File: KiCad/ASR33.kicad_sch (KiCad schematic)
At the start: 42 parts, among them J1 USB-C, J2 DC, J3 Power, J4 RUN, J5 Tx, J6 Rx, Q1 NX7002AK, SW1 SW_Push, U1 ESP32-WROOM-32, U2 FT231XQ, U3 NCR402U, U4 NCR402U, U5 LTV-355T, U6 LMR16006+FB, U7 QR

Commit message: Diode
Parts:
- D4: value D -> Schottky
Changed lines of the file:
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@@
     (in_bom yes) (on_board yes) (fields_autoplaced)
     (property "Reference" "D4" (id 0) (at 194.945 20.1635 0))
-    (property "Value" "D" (id 1) (at 194.945 22.9386 0))
+    (property "Value" "Schottky" (id 1) (at 194.945 22.9386 0))
     (property "Footprint" "Diode_SMD:D_1206_3216Metric" (id 2) (at 194.945 25.4 0)
       (effects (font (size 1.27 1.27)) hide)
@@
     )
     (path "/c30cd6e9-8158-45a7-96ab-d9fa2290e882"
-      (reference "D4") (unit 1) (value "D") (footprint "Diode_SMD:D_1206_3216Metric")
+      (reference "D4") (unit 1) (value "Schottky") (footprint "Diode_SMD:D_1206_3216Metric")
     )
     (path "/00000000-0000-0000-0000-0000610fe5d2"

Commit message: More tinkering
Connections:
- net MTR: now also U1.36 (IO22); no longer U1.37 (IO23)
- net PWR: now also U1.37 (IO23); no longer U1.36 (IO22)
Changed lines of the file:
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@@
     )
   )
-  (global_label "MTR" (shape input) (at 80.645 77.47 0) (fields_autoplaced)
+  (global_label "MTR" (shape input) (at 80.645 74.93 0) (fields_autoplaced)
     (effects (font (size 1.27 1.27)) (justify left))
-    (property "Intersheet References" "${INTERSHEET_REFS}" (id 0) (at 86.6582 77.3906 0)
+    (property "Intersheet References" "${INTERSHEET_REFS}" (id 0) (at 86.6582 74.8506 0)
       (effects (font (size 1.27 1.27)) (justify left) hide)
     )
@@
     )
   )
-  (global_label "PWR" (shape input) (at 80.645 74.93 0) (fields_autoplaced)
+  (global_label "PWR" (shape input) (at 80.645 77.47 0) (fields_autoplaced)
     (effects (font (size 1.27 1.27)) (justify left))
-    (property "Intersheet References" "${INTERSHEET_REFS}" (id 0) (at 86.9606 74.8506 0)
+    (property "Intersheet References" "${INTERSHEET_REFS}" (id 0) (at 86.9606 77.3906 0)
       (effects (font (size 1.27 1.27)) (justify left) hide)
     )

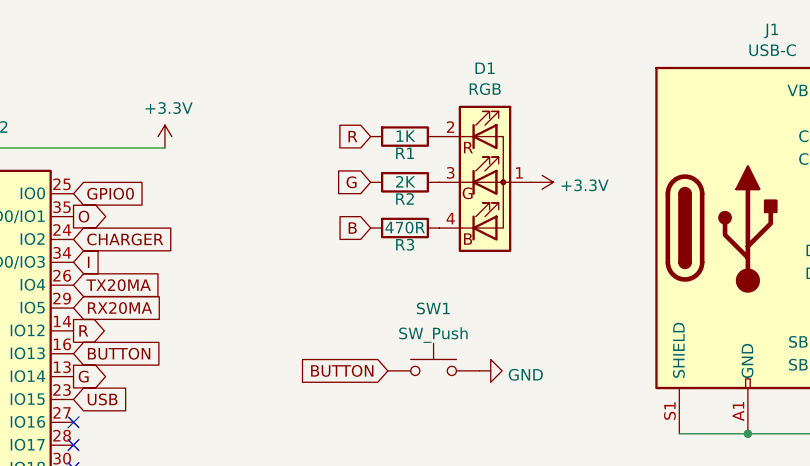
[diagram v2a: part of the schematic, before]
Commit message: Fix resistor values on LED
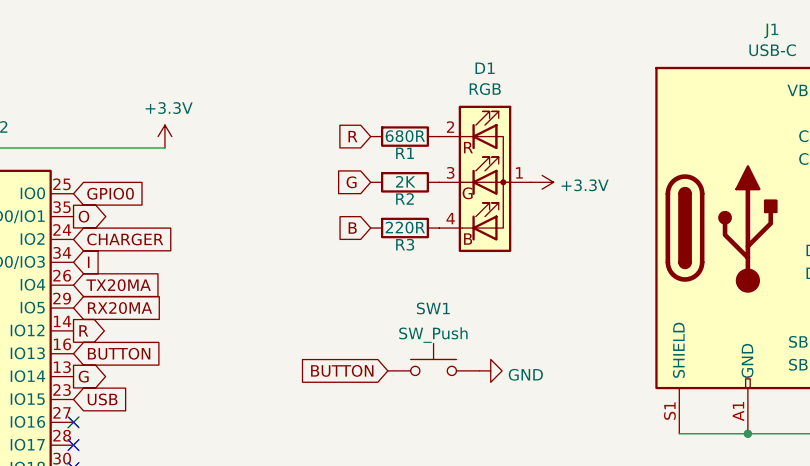
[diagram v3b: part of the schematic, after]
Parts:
- R1: value 1K -> 680R
- R3: value 470R -> 220R
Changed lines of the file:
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@@
     (in_bom yes) (on_board yes)
     (property "Reference" "R3" (id 0) (at 117.475 42.545 90))
-    (property "Value" "470R" (id 1) (at 117.475 40.64 90))
+    (property "Value" "220R" (id 1) (at 117.475 40.64 90))
     (property "Footprint" "RevK:R_0603" (id 2) (at 117.475 38.862 90)
       (effects (font (size 1.27 1.27)) hide)
@@
     (in_bom yes) (on_board yes)
     (property "Reference" "R1" (id 0) (at 117.475 32.385 90))
-    (property "Value" "1K" (id 1) (at 117.475 30.48 90))
+    (property "Value" "680R" (id 1) (at 117.475 30.48 90))
     (property "Footprint" "RevK:R_0603" (id 2) (at 117.475 28.702 90)
       (effects (font (size 1.27 1.27)) hide)
@@
     )
     (path "/00000000-0000-0000-0000-000060cf9e4d"
-      (reference "R1") (unit 1) (value "1K") (footprint "RevK:R_0603")
+      (reference "R1") (unit 1) (value "680R") (footprint "RevK:R_0603")
     )
     (path "/00000000-0000-0000-0000-000060cfbfaf"
@@
     )
     (path "/00000000-0000-0000-0000-000060a436c8"
-      (reference "R3") (unit 1) (value "470R") (footprint "RevK:R_0603")
+      (reference "R3") (unit 1) (value "220R") (footprint "RevK:R_0603")
     )
     (path "/00000000-0000-0000-0000-00006043a8ad"

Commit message: 60mA
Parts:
- removed C5: 110nF NF, Capacitor_SMD:C_1206_3216Metric, symbol Device:C
- removed C6: 10nF NF, RevK:C_0603, symbol Device:C
- removed JP1: Rx-RTN, RevK:SolderJumper-2_P1.3mm_Bridged2Bar_RoundedPad1.0x1.5mm, symbol Jumper:Jumper_2_Bridged
- removed R10: 470R NF, RevK:R_0603, symbol Device:R
- removed U5: LTV-355T, Package_SO:SO-4_4.4x3.6mm_P2.54mm, symbol Isolator:LTV-355T
- added JP1, JP2, JP4: 20R NF, RevK:Pad_1206_0805_Open, symbol Jumper:SolderJumper_2_Open
- added JP3: GND-Linked, RevK:Pad_1206_0805_Bridged, symbol Jumper:SolderJumper_2_Bridged
- added U5: LTV-356T, Package_SO:SO-4_4.4x3.6mm_P2.54mm, symbol Isolator:LTV-356T
- renumbered C7 to C5, C8 to C6, C9 to C7
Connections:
- net DC: now also JP1.2 (B), JP2.2 (B)
- net GND: now also JP3.1 (A), U5.3
- net RX20MA: now also U5.4
- net at J6.1 (Pin_1): now also JP3.2 (B), JP4.1 (A), U5.2
- net at J6.2 (Pin_2): now also JP4.2 (B), U5.1
- net at U3.6 (REXT): now also JP1.1 (A)
- net at U4.6 (REXT): now also JP2.1 (A)
- no-connect marks 24 -> 22
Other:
- moved on the sheet: Q1

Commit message: BOM fix
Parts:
- JP1, JP2, JP3, JP4: now left out of the parts list
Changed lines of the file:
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@@
   )
   (symbol (lib_id "Jumper:SolderJumper_2_Open") (at 245.745 137.16 90) (unit 1)
-    (in_bom yes) (on_board yes) (fields_autoplaced)
+    (in_bom no) (on_board yes) (fields_autoplaced)
     (property "Reference" "JP4" (id 0) (at 247.396 136.2515 90)
       (effects (font (size 1.27 1.27)) (justify right))
@@
   )
   (symbol (lib_id "Jumper:SolderJumper_2_Bridged") (at 239.395 148.59 90) (unit 1)
-    (in_bom yes) (on_board yes) (fields_autoplaced)
+    (in_bom no) (on_board yes) (fields_autoplaced)
     (property "Reference" "JP3" (id 0) (at 241.046 147.6815 90)
       (effects (font (size 1.27 1.27)) (justify right))
@@
   )
   (symbol (lib_id "Jumper:SolderJumper_2_Open") (at 177.8 103.505 90) (unit 1)
-    (in_bom yes) (on_board yes) (fields_autoplaced)
+    (in_bom no) (on_board yes) (fields_autoplaced)
     (property "Reference" "JP1" (id 0) (at 179.451 102.5965 90)
       (effects (font (size 1.27 1.27)) (justify right))
@@
   )
   (symbol (lib_id "Jumper:SolderJumper_2_Open") (at 177.8 132.715 90) (unit 1)
-    (in_bom yes) (on_board yes) (fields_autoplaced)
+    (in_bom no) (on_board yes) (fields_autoplaced)
     (property "Reference" "JP2" (id 0) (at 179.451 131.8065 90)
       (effects (font (size 1.27 1.27)) (justify right))

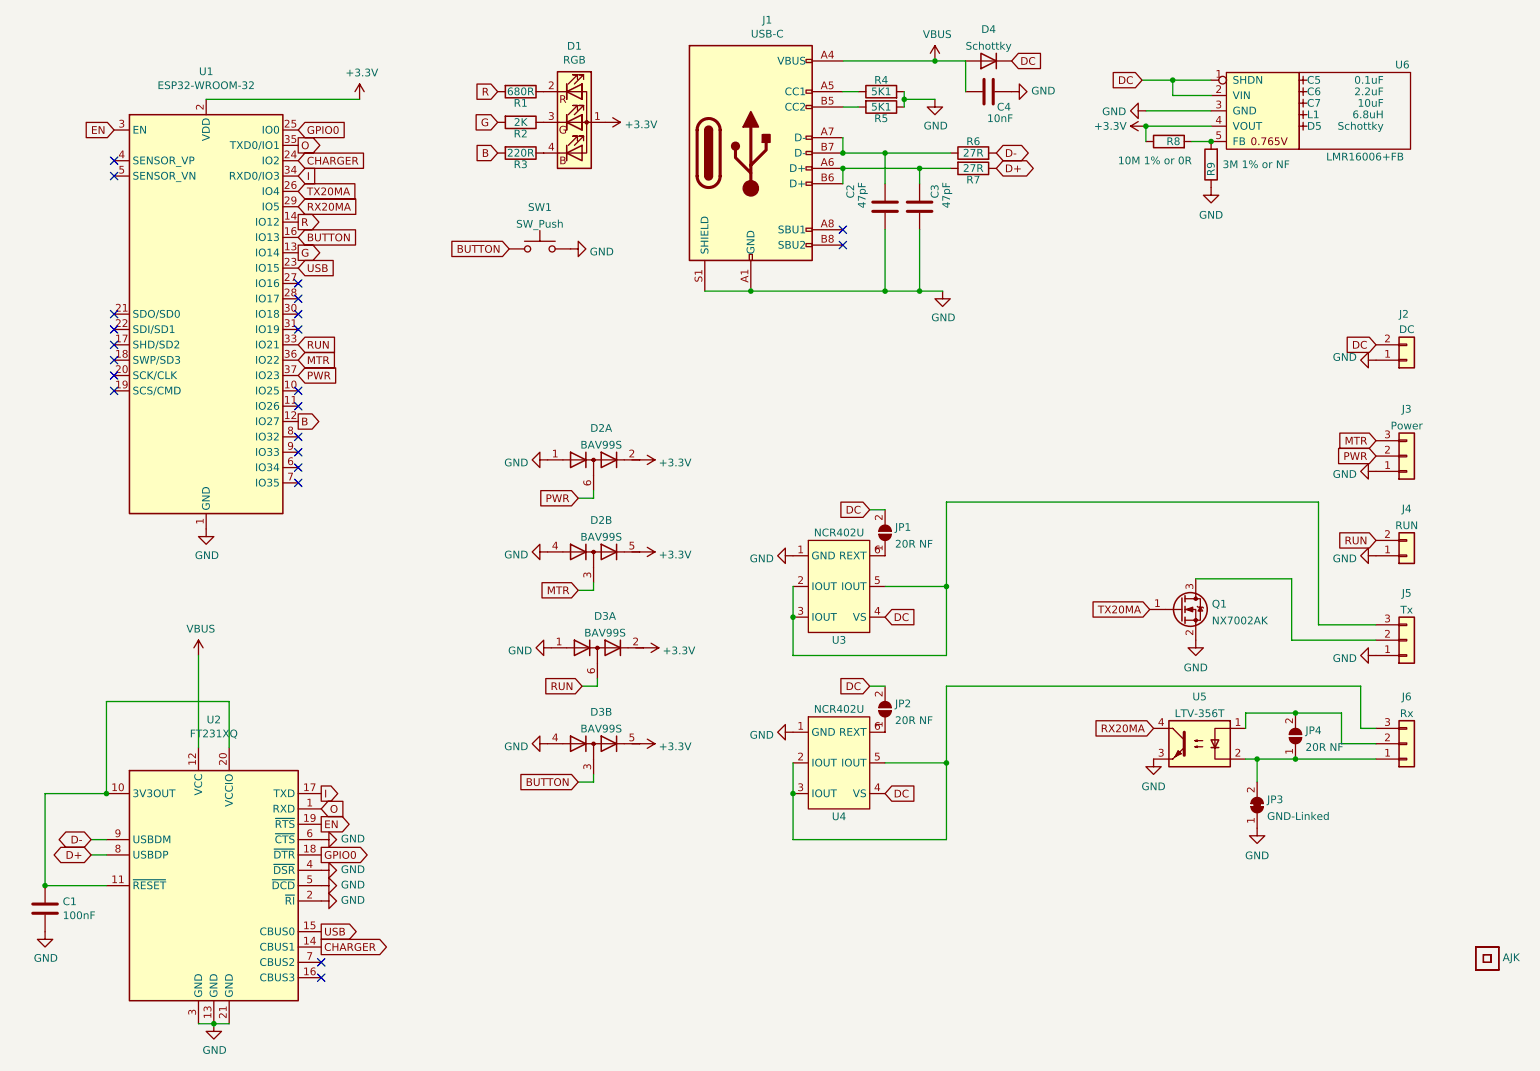
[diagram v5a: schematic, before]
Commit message: Corrected VBUS/DC working, and moved some GPIO to avoid problematic startup strapping.
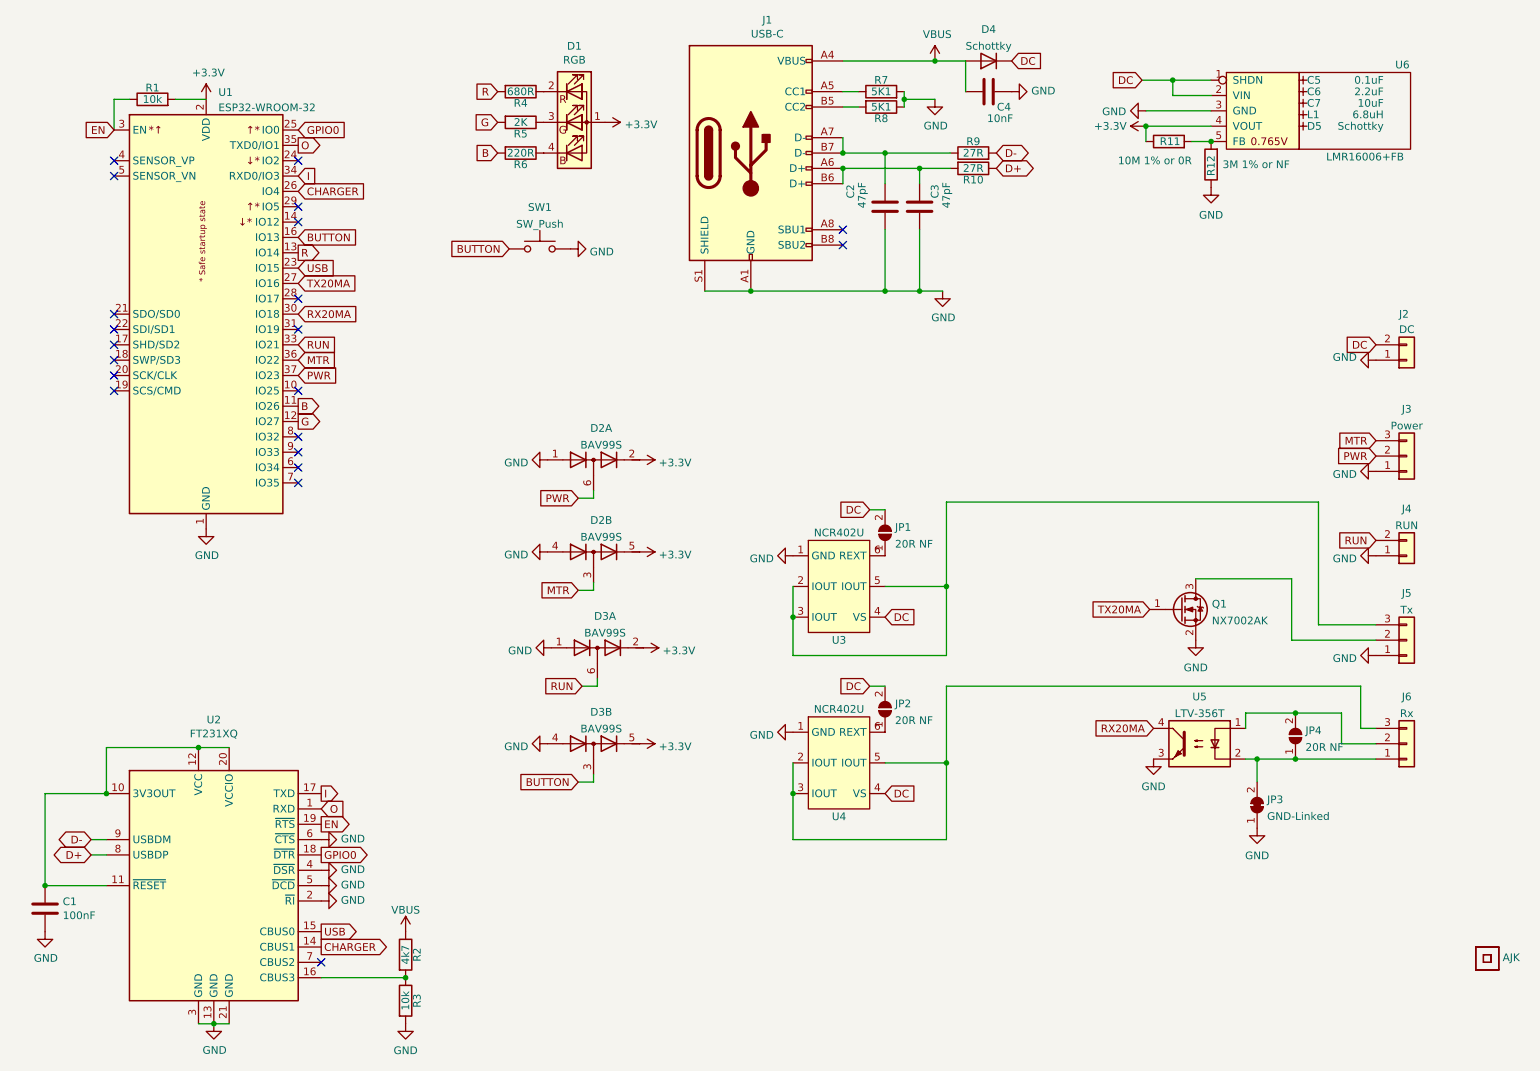
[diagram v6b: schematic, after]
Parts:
- removed U1: ESP32-WROOM-32, RevK:ESP32-WROOM-32, symbol RF_Module:ESP32-WROOM-32
- added R1, R3: 10k, RevK:R_0603, symbol Device:R
- added R2: 4k7, RevK:R_0603, symbol Device:R
- added U1: ESP32-WROOM-32, RF_Module:ESP32-WROOM-32, symbol RevK:ESP32-WROOM-32
- renumbered R7 to R10, R8 to R11, R9 to R12, R1 to R4, R2 to R5, R3 to R6, R4 to R7, R5 to R8, R6 to R9
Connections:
- net +3V3: now also R1.2, U1.2 (VDD)
- net B: now also U1.11 (IO26)
- net BUTTON: now also U1.16 (IO13)
- net CHARGER: now also U1.26 (IO4)
- net EN: now also R1.1, U1.3 (EN)
- net G: now also U1.12 (IO27)
- net GND: now also R3.2, U1.1 (GND), U1.15 (GND), U1.38 (GND), U1.39 (GND)
- net GPIO0: now also U1.25 (IO0)
- net I: now also U1.34 (RXD0/IO3)
- net MTR: now also U1.36 (IO22)
- net O: now also U1.35 (TXD0/IO1)
- net PWR: now also U1.37 (IO23)
- net R: now also U1.13 (IO14)
- net RUN: now also U1.33 (IO21)
- net RX20MA: now also U1.30 (IO18)
- net TX20MA: now also U1.27 (IO16)
- net USB: now also U1.23 (IO15)
- net VBUS: now also R2.1; no longer U2.12 (VCC)
- net at C1.1, U2.10 (3V3OUT), U2.11 (~{RESET})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: now also U2.12 (VCC)
- net at U2.16 (CBUS3): now also R2.2, R3.1
- no-connect marks 22 -> 21

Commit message: Library update
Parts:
- U1: footprint RF_Module:ESP32-WROOM-32 -> RevK:ESP32-WROOM-32
- U2: footprint RevK:QFN-20-1EP_4x4mm_P0.5mm_EP2.5x2.5mm -> Package_DFN_QFN:QFN-20-1EP_4x4mm_P0.5mm_EP2.5x2.5mm
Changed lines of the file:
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@@
     (property "Reference" "U2" (id 0) (at 66.675 134.4676 0))
     (property "Value" "FT231XQ" (id 1) (at 66.675 136.779 0))
-    (property "Footprint" "RevK:QFN-20-1EP_4x4mm_P0.5mm_EP2.5x2.5mm" (id 2) (at 100.965 182.245 0)
+    (property "Footprint" "Package_DFN_QFN:QFN-20-1EP_4x4mm_P0.5mm_EP2.5x2.5mm" (id 2) (at 100.965 182.245 0)
       (effects (font (size 1.27 1.27)) hide)
     )
@@
     (pin "5")
   )
-  (symbol (lib_name "NCR402U_1") (lib_id "RevK:NCR402U") (at 170.18 112.395 0) (unit 1)
+  (symbol (lib_id "RevK:NCR402U") (at 170.18 112.395 0) (unit 1)
     (in_bom yes) (on_board yes)
     (property "Reference" "U3" (id 0) (at 170.18 121.285 0))
@@
       (effects (font (size 1.27 1.27)) (justify left))
     )
-    (property "Footprint" "RF_Module:ESP32-WROOM-32" (id 2) (at 65.405 105.41 0)
+    (property "Footprint" "RevK:ESP32-WROOM-32" (id 2) (at 65.405 105.41 0)
       (effects (font (size 1.27 1.27)) hide)
     )
@@
     )
     (path "/de02af37-8d74-47e6-9bc1-9b4472e97a9f"
-      (reference "U1") (unit 1) (value "ESP32-WROOM-32") (footprint "RF_Module:ESP32-WROOM-32")
+      (reference "U1") (unit 1) (value "ESP32-WROOM-32") (footprint "RevK:ESP32-WROOM-32")
     )
     (path "/00000000-0000-0000-0000-000060849d1e"
-      (reference "U2") (unit 1) (value "FT231XQ") (footprint "RevK:QFN-20-1EP_4x4mm_P0.5mm_EP2.5x2.5mm")
+      (reference "U2") (unit 1) (value "FT231XQ") (footprint "Package_DFN_QFN:QFN-20-1EP_4x4mm_P0.5mm_EP2.5x2.5mm")
     )
     (path "/c9a08af4-5867-414a-a6a1-6cfb9a3fa372"
